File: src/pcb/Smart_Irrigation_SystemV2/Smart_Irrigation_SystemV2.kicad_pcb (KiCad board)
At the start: 4 copper layers, 100 x 55.5 mm, 133 parts, among them CN1 PJ-3136-3A, CN2 PJ-3136-3A, CN3 PJ-3136-3A, CN4 PJ-3136-3A, CN5 PJ-3136-3A, CN6 PJ-3136-3A, J1 USB_C_Receptacle_USB2.0_16P, J10 I2C, J11 I2C, J13 I2C, J14 SolarPanel, J15 I2C, J16 GPIO_Expander, J2 FPC_Connector, J6 I2C, J9 Battary Connection, Q1 MUN5211DW1, Q2 FDN340P, Q3 AO3400A, SW1 IO0 Switch, SW2 EN Switch, SW3 SW_Push, SW4 SW_Push, SW5 SW_Push, SW6 SW_Push, U1 CP2102N-Axx-xQFN28, U10 ADS1115IDGS, U11 PCA9536DP, U2 ESP32-WROOM-32, U3 ADS1115IDGS, U4 DS3231MZ, U5 TLV62568ADRL, U6 SN74LVC245APW, U7 TP4056-42-ESOP8, U8 TPS63001

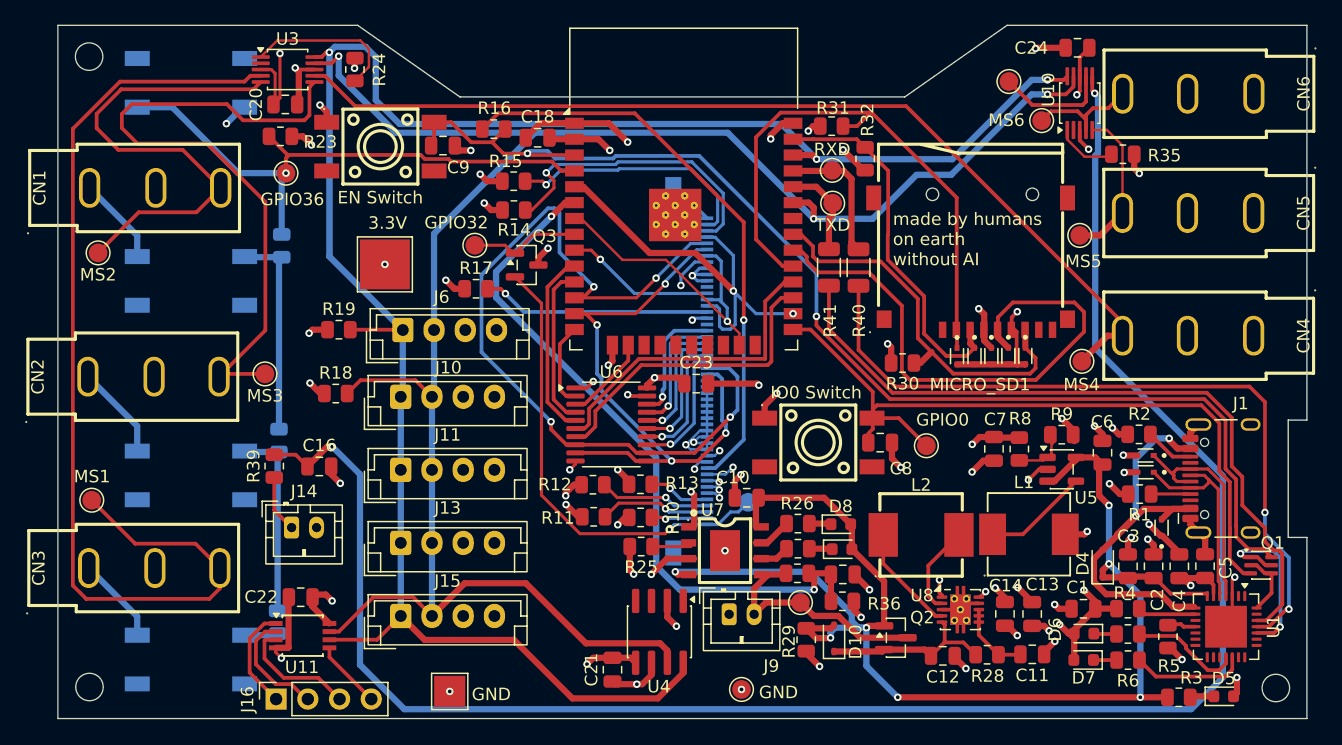
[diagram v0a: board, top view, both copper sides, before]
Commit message: fpc connector was in the wrong orientation. I moved it to the front, made a hole into the pcb, reorganized the libraries, rerouted everything, removed the unnecessary I2C outputs, rearranged components. Still need to work on the silkscreen, 3D models, move all other components to the front. time spend: 3h
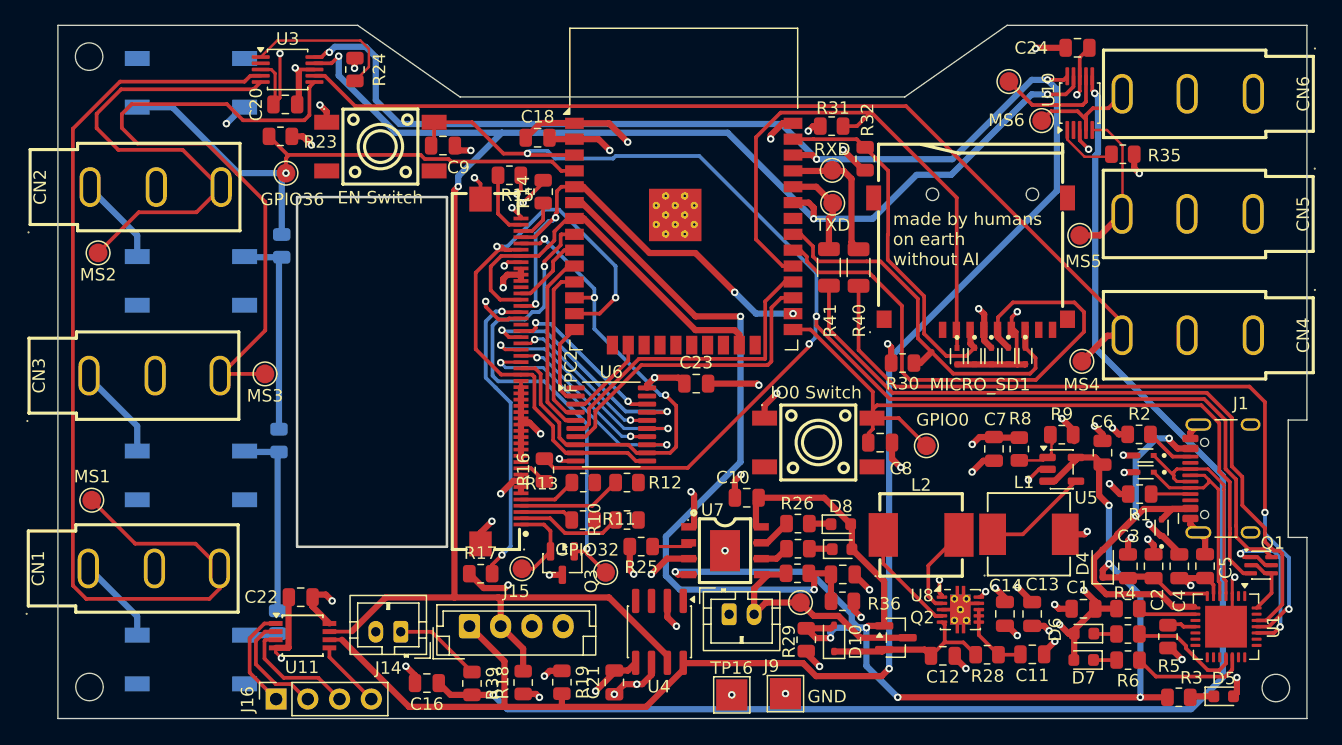
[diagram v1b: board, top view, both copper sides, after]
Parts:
- removed J10, J11, J13, J6: I2C, Connector_JST:JST_EH_B4B-EH-A_1x04_P2.50mm_Vertical
- removed J2: FPC_Connector, 5051105091:CON_5051105091_MOL
- removed TP14: GND, TestPoint:TestPoint_Pad_D1.5mm
- added FPC2: FPC-05FB-50PH20, C2856838:FPC-SMD_50P-P0.50_FPC-05FB-50PH20, F.Cu at (117.8, 104.1)
- TP10: moved to F.Cu
- TP16: footprint TestPoint:TestPoint_Pad_4.0x4.0mm -> TestPoint:TestPoint_Pad_2.5x2.5mm
- moved TP16 44.3 mm to (136.3, 130.0)
- moved R19 33.4 mm to (122.7, 129.0), turned to -90 degrees
- moved CN1 30.5 mm to (90.0, 119.9)
- moved TP1 28.2 mm to (126.2, 120.2)
- moved R16 27.6 mm to (121.3, 112.0), turned to -90 degrees
- moved R18 27.6 mm to (119.6, 129.0), turned to 90 degrees
- moved TP15 26.9 mm to (140.6, 129.9)
- moved Q3 24.0 mm to (122.7, 119.5), turned to -90 degrees
- moved R39 23.5 mm to (115.5, 129.1), turned to -90 degrees
- moved R17 22.8 mm to (116.2, 120.3)
- moved C16 19.4 mm to (111.9, 129.1), turned to 180 degrees
- moved TP10 18.9 mm to (119.5, 119.9), turned to 0 degrees
- moved CN3 15.4 mm to (90.1, 104.4)
- moved CN2 15.2 mm to (90.2, 89.3)
- moved J14 12.1 mm to (109.8, 125.0), turned to 180 degrees
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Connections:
- CN1 pad 4: /MS2 -> /MS1
- CN2 pad 4: /MS3 -> /MS2
- CN3 pad 4: /MS1 -> /MS3
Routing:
- net Net-(FPC2-Pad10): track 46.3 -> 2.31 mm, vias 1 -> 0
- net Net-(Q3-S): track 37.2 -> 7.07 mm, vias 1 -> 0
- net /GPIO32: track 8.86 -> 39.0 mm, vias 0 -> 2
- net /SolarPanel: track 148.3 -> 120.4 mm
- net /EN: track 96.5 -> 123.2 mm, vias 2 -> 3
- net /GPIO27: track 67.0 -> 42.4 mm, vias 4 -> 3
- net Net-(FPC2-Pad48): track 24.3 -> 3.49 mm, vias 1 -> 0
- net Net-(FPC2-Pad49): track 20.2 -> 5.28 mm, vias 1 -> 0
- net Net-(U6-B2): track 9.93 -> 19.3 mm, vias 1 -> 2
- net Net-(U6-B4): track 10.3 -> 19.6 mm, vias 1 -> 2
- net Net-(U6-B6): track 10.2 -> 19.2 mm, vias 1 -> 2
- net /SDA: track 158.2 -> 151.4 mm, vias 3 -> 4
- net Net-(FPC2-Pad35): track 18.4 -> 24.8 mm, vias 1 -> 2
- net +3.3V: track 87.9 -> 81.5 mm, vias 34 -> 30
- net /GPIO33: track 11.8 -> 6.15 mm, vias 1 -> 0
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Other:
- outline, holes or cut-outs redrawn

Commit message: moved silkscreen and replaced buttons with smd ones
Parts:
- R20, R21, R22: moved to F.Cu
- SW3, SW4, SW5, SW6: footprint C83206:KEY-SMD_4P-L6.0-W6.0-P3.90-LS9.0 -> Button_Switch_THT:SW_PUSH_6mm_H5mm; moved to F.Cu
- moved SW4 4.87 mm to (88.9, 109.8), turned to 0 degrees
- moved SW5 4.59 mm to (88.9, 94.8), turned to 0 degrees
- moved SW3 4.43 mm to (88.9, 125.5), turned to 0 degrees
- moved SW6 3.61 mm to (95.4, 83.7), turned to 180 degrees
- moved R20 3.02 mm to (98.4, 121.6)
- moved R22 1.79 mm to (98.5, 93.8)
- moved R21 1.62 mm to (98.6, 108.9)
- moved TP8 0.54 mm to (98.4, 104.2)
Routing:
- net GND: track 169.6 -> 153.8 mm, vias 53 -> 54
- net +3.3V: track 81.5 -> 93.3 mm, vias 30 -> 35
- net Net-(R20-Pad1): track 2.69 -> 10.6 mm
- net Net-(R21-Pad2): track 16.8 -> 23.3 mm
- net Net-(R20-Pad2): track 15.4 -> 20.1 mm
- net /GPIO36: track 46.3 -> 43.8 mm, vias 1 -> 0
- net /MS3: track 53.2 -> 52.4 mm
